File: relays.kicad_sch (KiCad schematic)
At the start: 11 parts, among them K1 J107F1AS123VDC.36, K2 J107F1AS123VDC.36, K3 J107F1AS123VDC.36, K4 J107F1AS123VDC.36, K5 J107F1AS123VDC.36, Q1 2N2222A, Q2 2N2222A, Q3 2N2222A, Q4 2N2222A, Q5 2N2222A

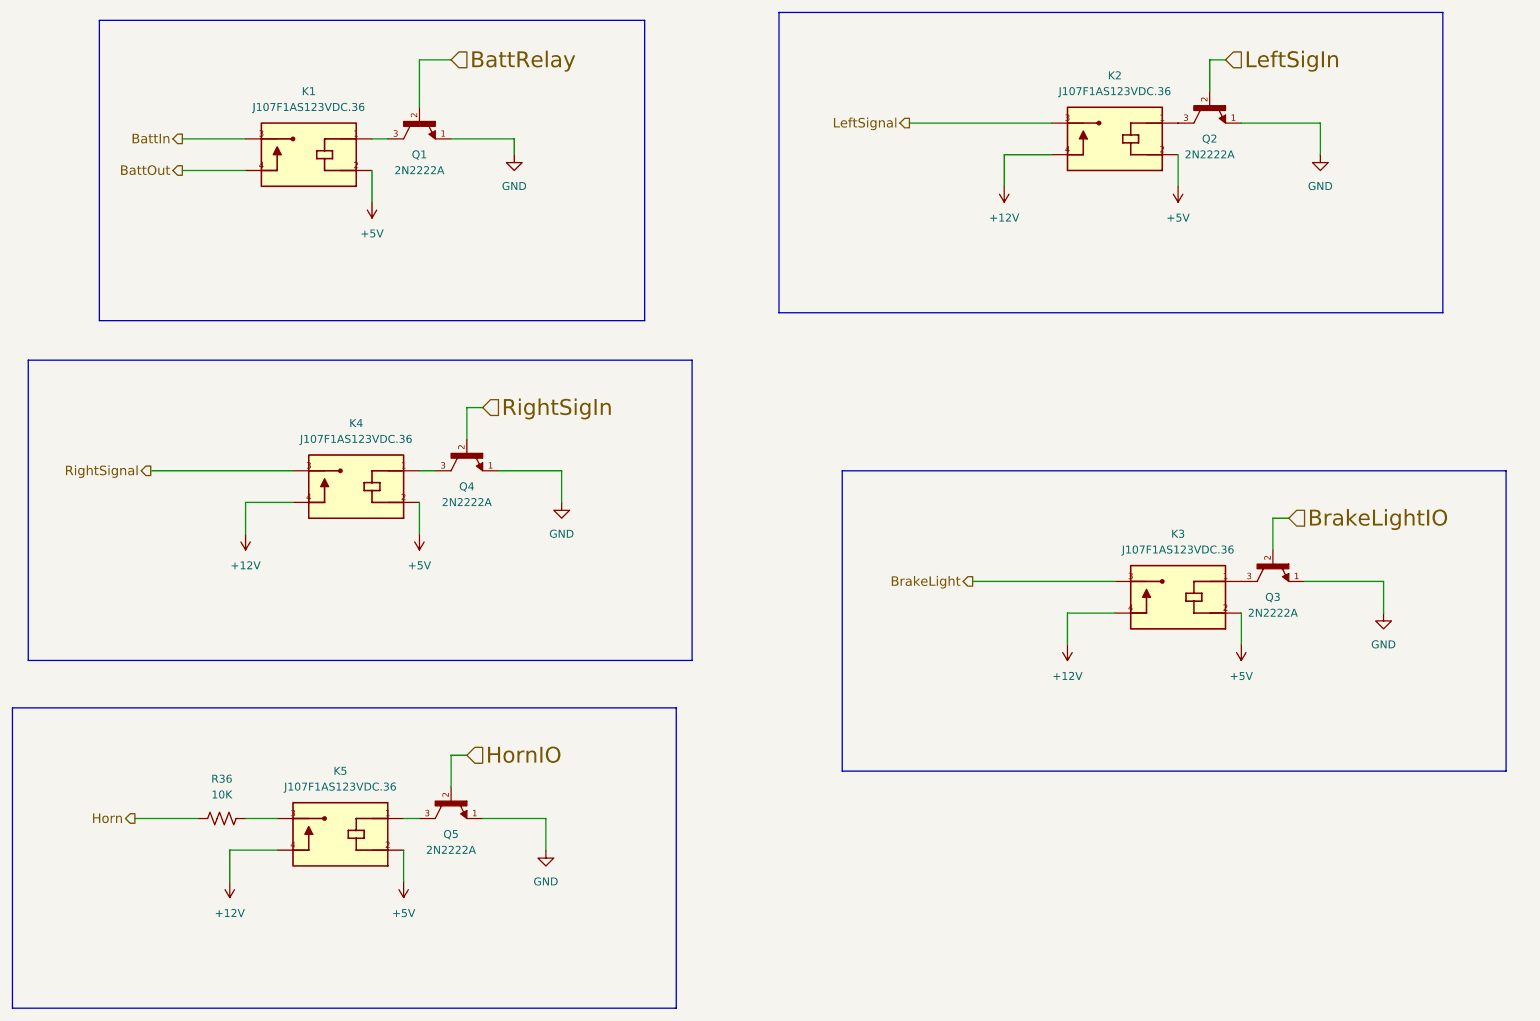
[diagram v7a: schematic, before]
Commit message: fixed relays
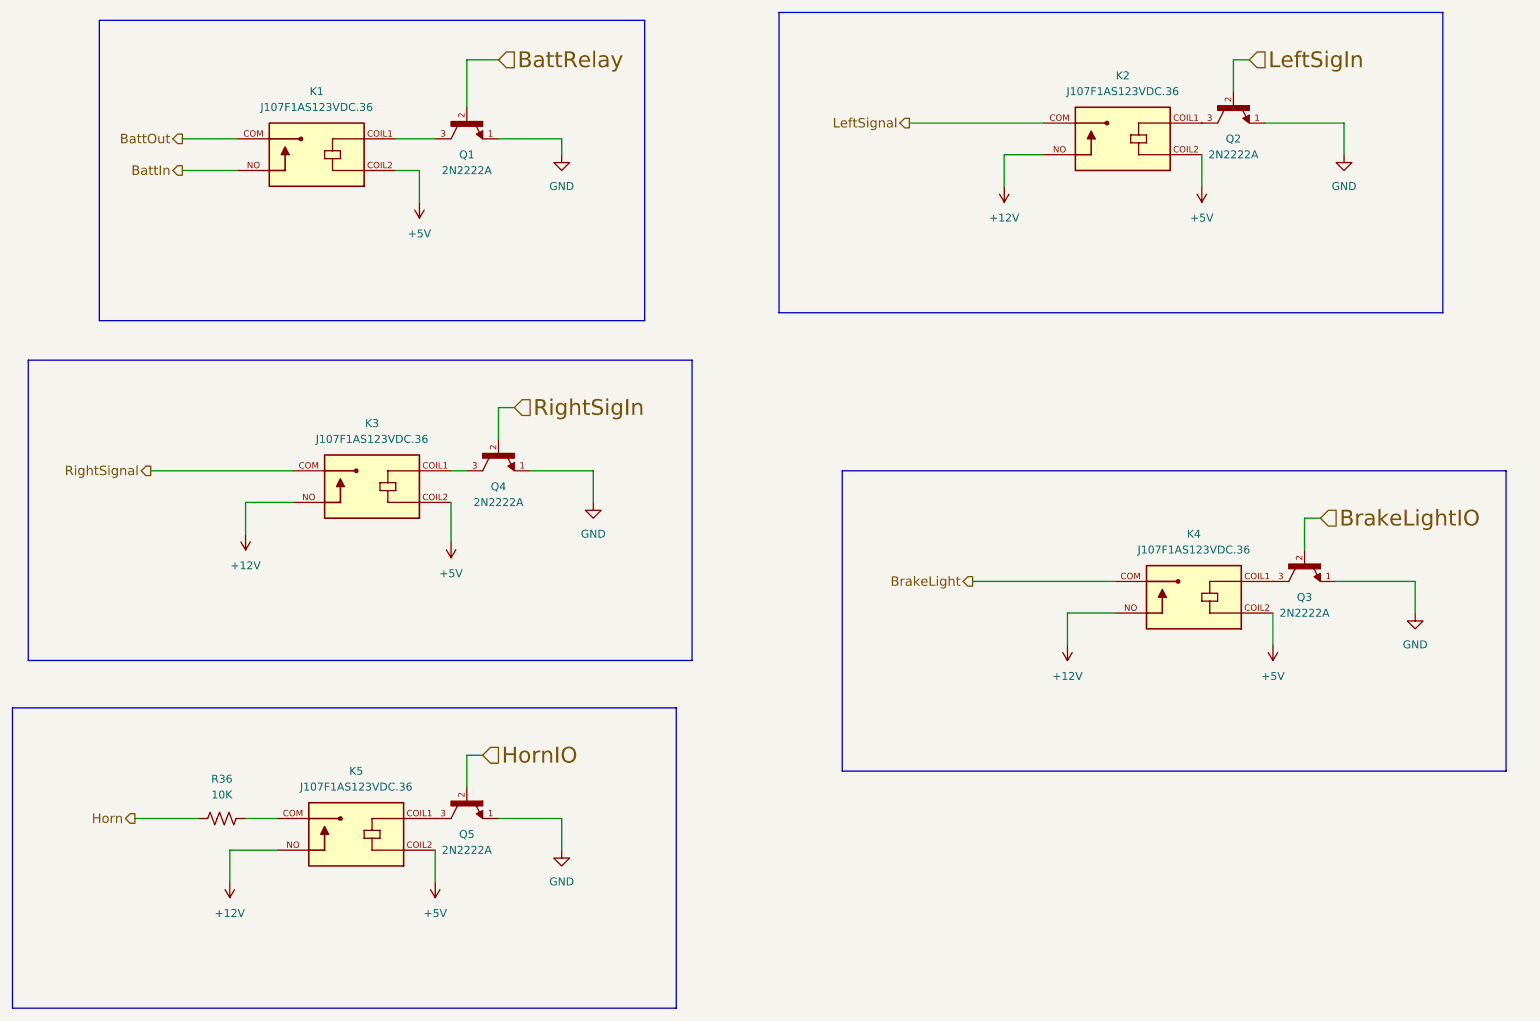
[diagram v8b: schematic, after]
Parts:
- removed K1, K2, K3, K4, K5: J107F1AS123VDC.36, PRE29-5V-S-450-1A-E:RELAY_PRE29-5V-S-450-1A-E, symbol PRE29-5V-S-450-1A-E:PRE29-5V-S-450-1A-E
- added K1, K2, K3, K4, K5: J107F1AS123VDC.36, J107F1AS123VDC.36:RELAY_J107F1AS123VDC.36, symbol J107F1AS123VDC.36:J107F1AS123VDC.36
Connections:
- net +12V: now also K2.NO, K3.NO, K4.NO, K5.NO
- net +5V: now also K1.COIL2, K2.COIL2, K3.COIL2, K4.COIL2, K5.COIL2
- net BattIn: now also K1.NO
- net BattOut: now also K1.COM
- net BrakeLight: now also K4.COM
- net LeftSignal: now also K2.COM
- net RightSignal: now also K3.COM
- net at Q2.3: now also K2.COIL1
- net at Q1.3: now also K1.COIL1
- net at Q5.3: now also K5.COIL1
- net at R36.2: now also K5.COM
- net at Q4.3: now also K3.COIL1
- net at Q3.3: now also K4.COIL1
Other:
- moved on the sheet: Q1, Q2, Q3, Q4, Q5
